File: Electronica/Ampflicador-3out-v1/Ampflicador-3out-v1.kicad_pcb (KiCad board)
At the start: 2 copper layers, 13 x 1.4 mm, 24 parts, among them U1 LM386

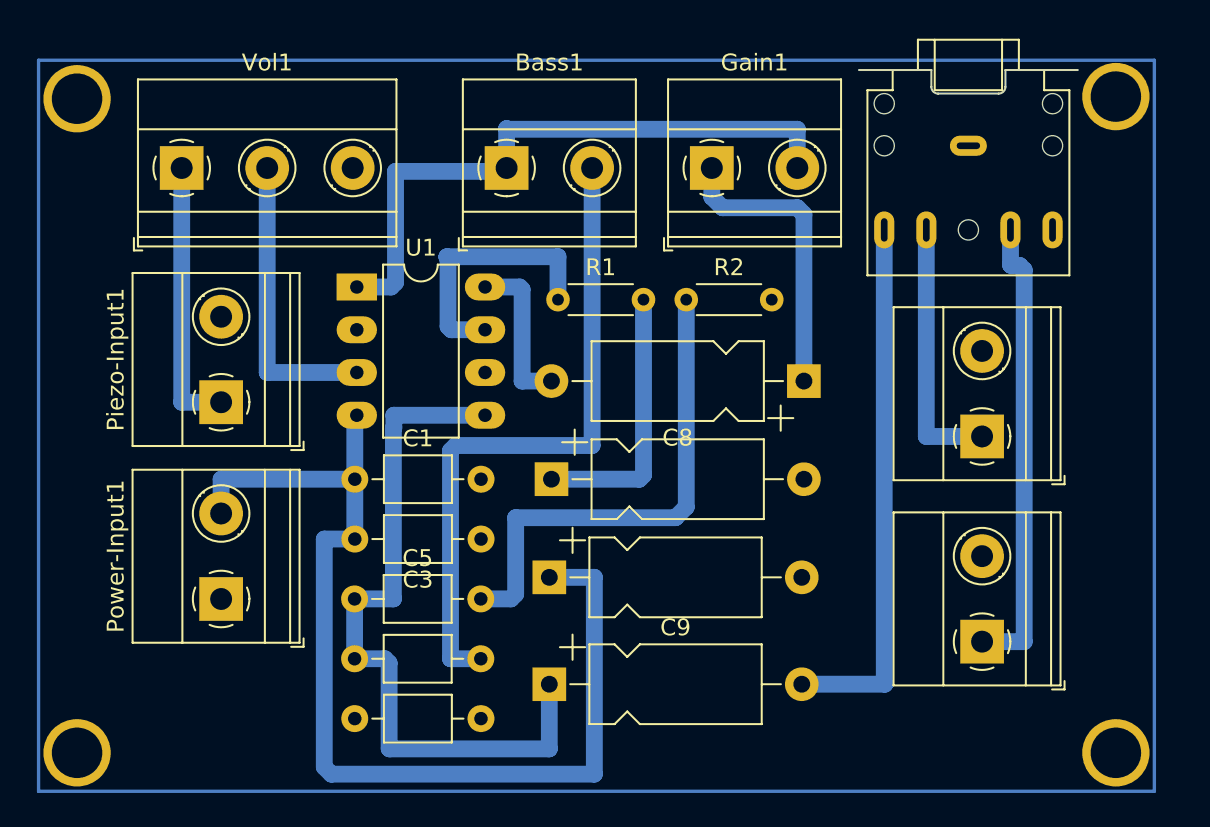
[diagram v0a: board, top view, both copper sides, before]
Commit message: Amp v1 sin plano de masa
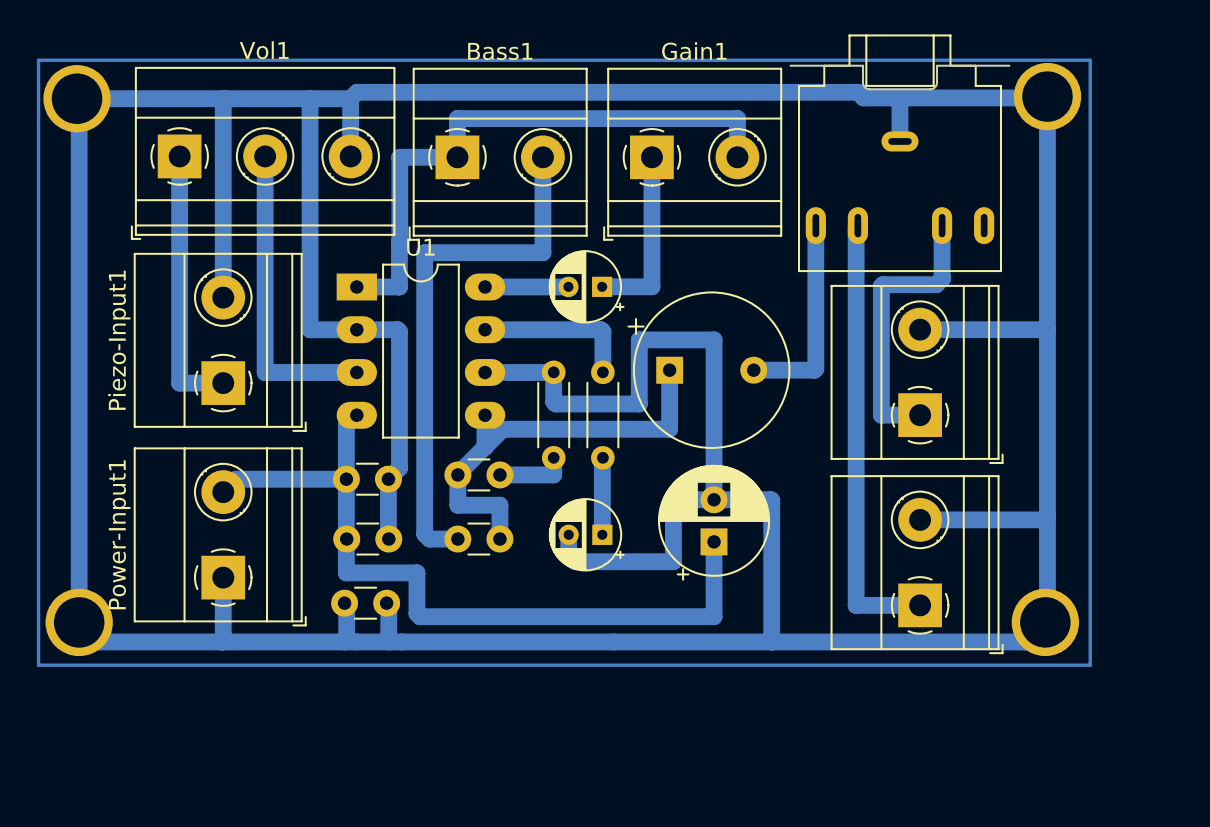
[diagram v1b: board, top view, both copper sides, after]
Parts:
- C1, C2, C3, C4, C5: footprint Capacitor_THT:C_Axial_L3.8mm_D2.6mm_P7.50mm_Horizontal -> Capacitor_THT:C_Disc_D3.0mm_W1.6mm_P2.50mm
- C6: footprint Capacitor_THT:CP_Axial_L10.0mm_D4.5mm_P15.00mm_Horizontal -> Capacitor_THT:CP_Radial_D6.3mm_P2.50mm
- C7, C8: footprint Capacitor_THT:CP_Axial_L10.0mm_D4.5mm_P15.00mm_Horizontal -> Capacitor_THT:CP_Radial_D4.0mm_P2.00mm
- C9: value 100µF -> 1000µF; footprint Capacitor_THT:CP_Axial_L10.0mm_D4.5mm_P15.00mm_Horizontal -> Capacitor_THT:CP_Radial_Tantal_D9.0mm_P5.00mm
- moved C9 20.0 mm to (49.7, 30.6)
- moved Output-Jack-6.5 14.0 mm to (64.6, 33.3)
- moved C8 13.2 mm to (45.7, 25.7)
- moved R2 12.3 mm to (42.8, 35.8), turned to 90 degrees
- moved Output-Speaker1 10.7 mm to (64.6, 44.6)
- moved C6 10.0 mm to (52.3, 40.8), turned to 90 degrees
- moved C5 9.59 mm to (37.1, 36.8)
- moved ? 8.81 mm to (72.0, 45.6)
- moved ? 7.75 mm to (14.6, 45.6)
- moved C4 7.24 mm to (37.1, 40.6), turned to 0 degrees
- moved C2 6.88 mm to (30.4, 44.5)
- moved C3 5.48 mm to (33.0, 40.6)
- moved R1 5.08 mm to (45.7, 30.7), turned to -90 degrees
- moved C7 4.48 mm to (45.7, 40.4), turned to 180 degrees
- moved Output-Jack-3.5 4.07 mm to (63.4, 17.0)
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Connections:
- Output-Jack-3.5 pad R: unconnected-(Output-Jack-3.5-PadS) -> (no net)
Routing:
- net GND: track 0.00 -> 306.7 mm
- net Net-(C5-Pad2): track 29.7 -> 4.21 mm
- net Net-(C9-Pad2): track 31.9 -> 12.2 mm
- net Net-(Power-Input1-Pin_2): track 63.3 -> 46.0 mm
- net Net-(C4-Pad2): track 42.8 -> 27.2 mm
- net Net-(C7-Pad1): track 16.0 -> 4.59 mm
- net Net-(Output-Speaker1-Pin_1): track 15.8 -> 26.4 mm
- net Net-(Output-Jack-6.5-Pin_1): track 27.4 -> 16.9 mm
- net Net-(Bass1-Pin_2): track 39.2 -> 31.5 mm
- net Net-(Gain1-Pin_1): track 17.5 -> 10.7 mm
- net Net-(U1-BYPASS): track 15.6 -> 9.66 mm
- net Net-(C8-Pad2): track 9.45 -> 5.01 mm
- net Net-(Bass1-Pin_1): track 37.6 -> 34.9 mm
- net Net-(U1-+): track 17.5 -> 18.3 mm
- added copper zone on B.Cu, net GND

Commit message: Amp V1
Plano de masa
Cambiar pads de los cap. de 10microF
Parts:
- C1, C2, C3, C4, C5: footprint Capacitor_THT:C_Disc_D3.0mm_W1.6mm_P2.50mm -> Capacitor_THT:C_Disc_D5.0mm_W2.5mm_P2.50mm
- C6: footprint Capacitor_THT:CP_Radial_D6.3mm_P2.50mm -> Capacitor_THT:CP_Radial_D5.0mm_P2.50mm
- C7, C8: footprint Capacitor_THT:CP_Radial_D4.0mm_P2.00mm -> Capacitor_THT:CP_Radial_D4.0mm_P1.50mm
- moved C5 0.17 mm to (37.1, 37.0)
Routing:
- net GND: track 306.7 -> 0.03 mm
- net Net-(C4-Pad2): track 27.2 -> 25.6 mm
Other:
- board outline removed
